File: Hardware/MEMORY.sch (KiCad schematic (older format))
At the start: 9 parts, among them J37 Micro_SD_Card, U45 M24C64-WDW6TP

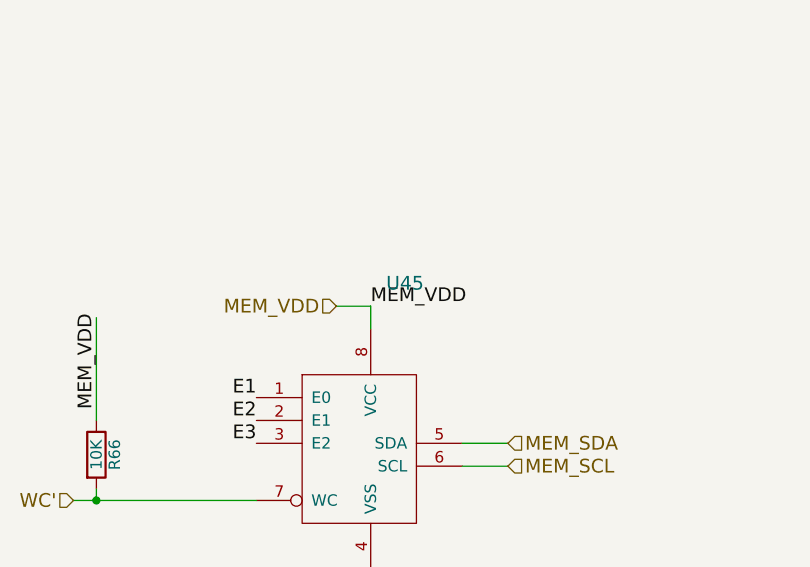
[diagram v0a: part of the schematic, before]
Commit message: Finished RLC bom stuff
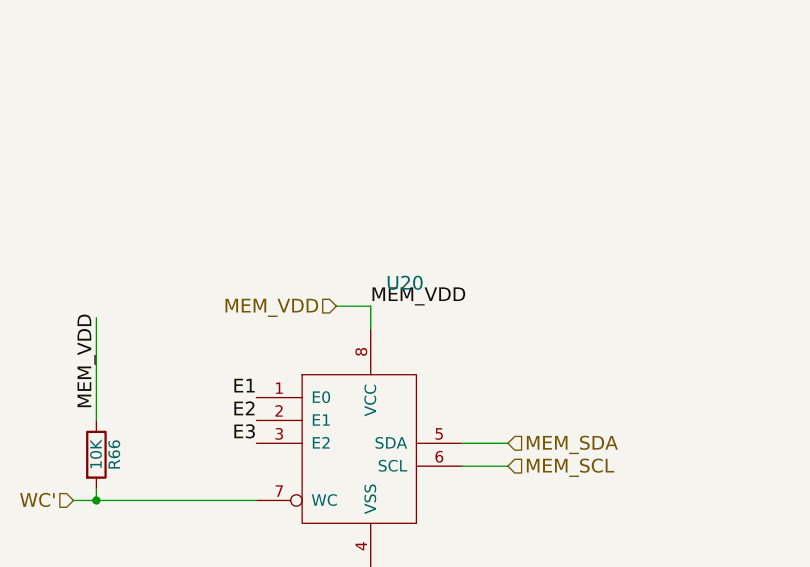
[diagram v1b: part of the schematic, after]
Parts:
- R60, R62, R64: part_num (none) -> RESS-001
- R61, R63, R65, R66: part_num (none) -> RESS-005
- renumbered U45 to U20
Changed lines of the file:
@@
 	7300 2100 7300 2400
 $Comp
-L M24C64-WDW6TP U45
+L M24C64-WDW6TP U20
 U 1 1 592069C1
 P 5300 5000
-F 0 "U45" H 5300 5450 60  0000 C CNN
+F 0 "U20" H 5300 5450 60  0000 C CNN
 F 1 "M24C64-WDW6TP" H 5250 4100 60  0000 C CNN
 F 2 "" H 5300 5000 60  0001 C CNN
@@
 Text HLabel 3850 5500 0    60   Input ~ 0
 WC'
-$Comp
-L R R66
-U 1 1 59206A6D
-P 3950 5300
-F 0 "R66" V 4030 5300 50  0000 C CNN
-F 1 "10K" V 3950 5300 50  0000 C CNN
-F 2 "" V 3880 5300 50  0001 C CNN
-F 3 "" H 3950 5300 50  0001 C CNN
-	1    3950 5300
-	1    0    0    -1
-$EndComp
 Wire Wire Line
 	3950 5450 3950 5500
@@
 F 2 "" V 1580 5650 50  0001 C CNN
 F 3 "" H 1650 5650 50  0001 C CNN
+F 4 "RESS-005" V 1650 5650 60  0001 C CNN "part_num"
 	1    1650 5650
-	1    0    0    -1
-$EndComp
-$Comp
-L R R63
-U 1 1 59206CAA
-P 1900 5650
-F 0 "R63" V 1980 5650 50  0000 C CNN
-F 1 "10K" V 1900 5650 50  0000 C CNN
-F 2 "" V 1830 5650 50  0001 C CNN
-F 3 "" H 1900 5650 50  0001 C CNN
-	1    1900 5650
-	1    0    0    -1
-$EndComp
-$Comp
-L R R65
-U 1 1 59206CD2
-P 2150 5650
-F 0 "R65" V 2230 5650 50  0000 C CNN
-F 1 "10K" V 2150 5650 50  0000 C CNN
-F 2 "" V 2080 5650 50  0001 C CNN
-F 3 "" H 2150 5650 50  0001 C CNN
-	1    2150 5650
 	1    0    0    -1
 $EndComp
@@
 F 2 "" V 1580 5100 50  0001 C CNN
 F 3 "" H 1650 5100 50  0001 C CNN
+F 4 "RESS-001" V 1650 5100 60  0001 C CNN "part_num"
 	1    1650 5100
-	1    0    0    -1
-$EndComp
-$Comp
-L R R62
-U 1 1 59206D6A
-P 1900 5100
-F 0 "R62" V 1980 5100 50  0000 C CNN
-F 1 "0" V 1900 5100 50  0000 C CNN
-F 2 "" V 1830 5100 50  0001 C CNN
-F 3 "" H 1900 5100 50  0001 C CNN
-	1    1900 5100
-	1    0    0    -1
-$EndComp
-$Comp
-L R R64
-U 1 1 59206D71
-P 2150 5100
-F 0 "R64" V 2230 5100 50  0000 C CNN
-F 1 "0" V 2150 5100 50  0000 C CNN
-F 2 "" V 2080 5100 50  0001 C CNN
-F 3 "" H 2150 5100 50  0001 C CNN
-	1    2150 5100
 	1    0    0    -1
 $EndComp
@@
 	1    0    0    -1
 $EndComp
+$Comp
+L R R63
+U 1 1 59596B34
+P 1900 5650
+F 0 "R63" V 1980 5650 50  0000 C CNN
+F 1 "10K" V 1900 5650 50  0000 C CNN
+F 2 "" V 1830 5650 50  0001 C CNN
+F 3 "" H 1900 5650 50  0001 C CNN
+F 4 "RESS-005" V 1900 5650 60  0001 C CNN "part_num"
+	1    1900 5650
+	1    0    0    -1
+$EndComp
+$Comp
+L R R65
+U 1 1 59596B68
+P 2150 5650
+F 0 "R65" V 2230 5650 50  0000 C CNN
+F 1 "10K" V 2150 5650 50  0000 C CNN
+F 2 "" V 2080 5650 50  0001 C CNN
+F 3 "" H 2150 5650 50  0001 C CNN
+F 4 "RESS-005" V 2150 5650 60  0001 C CNN "part_num"
+	1    2150 5650
+	1    0    0    -1
+$EndComp
+$Comp
+L R R62
+U 1 1 59596BE6
+P 1900 5100
+F 0 "R62" V 1980 5100 50  0000 C CNN
+F 1 "0" V 1900 5100 50  0000 C CNN
+F 2 "" V 1830 5100 50  0001 C CNN
+F 3 "" H 1900 5100 50  0001 C CNN
+F 4 "RESS-001" V 1900 5100 60  0001 C CNN "part_num"
+	1    1900 5100
+	1    0    0    -1
+$EndComp
+$Comp
+L R R64
+U 1 1 59596C1A
+P 2150 5100
+F 0 "R64" V 2230 5100 50  0000 C CNN
+F 1 "0" V 2150 5100 50  0000 C CNN
+F 2 "" V 2080 5100 50  0001 C CNN
+F 3 "" H 2150 5100 50  0001 C CNN
+F 4 "RESS-001" V 2150 5100 60  0001 C CNN "part_num"
+	1    2150 5100
+	1    0    0    -1
+$EndComp
+$Comp
+L R R66
+U 1 1 59596D32
+P 3950 5300
+F 0 "R66" V 4030 5300 50  0000 C CNN
+F 1 "10K" V 3950 5300 50  0000 C CNN
+F 2 "" V 3880 5300 50  0001 C CNN
+F 3 "" H 3950 5300 50  0001 C CNN
+F 4 "RESS-005" V 3950 5300 60  0001 C CNN "part_num"
+	1    3950 5300
+	1    0    0    -1
+$EndComp

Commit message: Added ressistor footprint
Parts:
- R60, R61, R62, R63, R64, R65, R66: footprint (none) -> Resistors_SMD:R_0603_HandSoldering
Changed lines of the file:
@@
 F 0 "R61" V 1730 5650 50  0000 C CNN
 F 1 "10K" V 1650 5650 50  0000 C CNN
-F 2 "" V 1580 5650 50  0001 C CNN
+F 2 "Resistors_SMD:R_0603_HandSoldering" V 1580 5650 50  0001 C CNN
 F 3 "" H 1650 5650 50  0001 C CNN
 F 4 "RESS-005" V 1650 5650 60  0001 C CNN "part_num"
@@
 F 0 "R60" V 1730 5100 50  0000 C CNN
 F 1 "0" V 1650 5100 50  0000 C CNN
-F 2 "" V 1580 5100 50  0001 C CNN
+F 2 "Resistors_SMD:R_0603_HandSoldering" V 1580 5100 50  0001 C CNN
 F 3 "" H 1650 5100 50  0001 C CNN
 F 4 "RESS-001" V 1650 5100 60  0001 C CNN "part_num"
@@
 F 0 "R63" V 1980 5650 50  0000 C CNN
 F 1 "10K" V 1900 5650 50  0000 C CNN
-F 2 "" V 1830 5650 50  0001 C CNN
+F 2 "Resistors_SMD:R_0603_HandSoldering" V 1830 5650 50  0001 C CNN
 F 3 "" H 1900 5650 50  0001 C CNN
 F 4 "RESS-005" V 1900 5650 60  0001 C CNN "part_num"
@@
 F 0 "R65" V 2230 5650 50  0000 C CNN
 F 1 "10K" V 2150 5650 50  0000 C CNN
-F 2 "" V 2080 5650 50  0001 C CNN
+F 2 "Resistors_SMD:R_0603_HandSoldering" V 2080 5650 50  0001 C CNN
 F 3 "" H 2150 5650 50  0001 C CNN
 F 4 "RESS-005" V 2150 5650 60  0001 C CNN "part_num"
@@
 F 0 "R62" V 1980 5100 50  0000 C CNN
 F 1 "0" V 1900 5100 50  0000 C CNN
-F 2 "" V 1830 5100 50  0001 C CNN
+F 2 "Resistors_SMD:R_0603_HandSoldering" V 1830 5100 50  0001 C CNN
 F 3 "" H 1900 5100 50  0001 C CNN
 F 4 "RESS-001" V 1900 5100 60  0001 C CNN "part_num"
@@
 F 0 "R64" V 2230 5100 50  0000 C CNN
 F 1 "0" V 2150 5100 50  0000 C CNN
-F 2 "" V 2080 5100 50  0001 C CNN
+F 2 "Resistors_SMD:R_0603_HandSoldering" V 2080 5100 50  0001 C CNN
 F 3 "" H 2150 5100 50  0001 C CNN
 F 4 "RESS-001" V 2150 5100 60  0001 C CNN "part_num"
@@
 F 0 "R66" V 4030 5300 50  0000 C CNN
 F 1 "10K" V 3950 5300 50  0000 C CNN
-F 2 "" V 3880 5300 50  0001 C CNN
+F 2 "Resistors_SMD:R_0603_HandSoldering" V 3880 5300 50  0001 C CNN
 F 3 "" H 3950 5300 50  0001 C CNN
 F 4 "RESS-005" V 3950 5300 60  0001 C CNN "part_num"

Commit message: PCB?!
Added initial PCB file with ratsnest. footprint library still needs to
be setup.
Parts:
- U20: footprint (none) -> Housings_SSOP:TSSOP-8_4.4x3mm_Pitch0.65mm
- renumbered R60 to R85, R61 to R86, R62 to R87, R63 to R88, R64 to R89, R65 to R90, R66 to R91
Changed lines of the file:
@@
 $EndDescr
 $Comp
-L GND #PWR054
+L GND #PWR55
 U 1 1 5920672F
 P 9100 2500
-F 0 "#PWR054" H 9100 2250 50  0001 C CNN
+F 0 "#PWR55" H 9100 2250 50  0001 C CNN
 F 1 "GND" H 9100 2350 50  0000 C CNN
 F 2 "" H 9100 2500 50  0001 C CNN
@@
 	6950 2200 7400 2200
 $Comp
-L GND #PWR055
+L GND #PWR54
 U 1 1 592067B5
 P 7300 2400
-F 0 "#PWR055" H 7300 2150 50  0001 C CNN
+F 0 "#PWR54" H 7300 2150 50  0001 C CNN
 F 1 "GND" H 7300 2250 50  0000 C CNN
 F 2 "" H 7300 2400 50  0001 C CNN
@@
 	7300 2100 7300 2400
 $Comp
-L M24C64-WDW6TP U20
-U 1 1 592069C1
-P 5300 5000
-F 0 "U20" H 5300 5450 60  0000 C CNN
-F 1 "M24C64-WDW6TP" H 5250 4100 60  0000 C CNN
-F 2 "" H 5300 5000 60  0001 C CNN
-F 3 "" H 5300 5450 60  0001 C CNN
-F 4 "MEMM-001" H 5300 5000 60  0001 C CNN "part_num"
-	1    5300 5000
-	1    0    0    -1
-$EndComp
-$Comp
-L GND #PWR056
+L GND #PWR53
 U 1 1 592069E4
 P 5150 5850
-F 0 "#PWR056" H 5150 5600 50  0001 C CNN
+F 0 "#PWR53" H 5150 5600 50  0001 C CNN
 F 1 "GND" H 5150 5700 50  0000 C CNN
 F 2 "" H 5150 5850 50  0001 C CNN
@@
 E3
 $Comp
-L R R61
+L R R86
 U 1 1 59206C6F
 P 1650 5650
-F 0 "R61" V 1730 5650 50  0000 C CNN
+F 0 "R86" V 1730 5650 50  0000 C CNN
 F 1 "10K" V 1650 5650 50  0000 C CNN
 F 2 "Resistors_SMD:R_0603_HandSoldering" V 1580 5650 50  0001 C CNN
@@
 $EndComp
 $Comp
-L R R60
+L R R85
 U 1 1 59206D63
 P 1650 5100
-F 0 "R60" V 1730 5100 50  0000 C CNN
+F 0 "R85" V 1730 5100 50  0000 C CNN
 F 1 "0" V 1650 5100 50  0000 C CNN
 F 2 "Resistors_SMD:R_0603_HandSoldering" V 1580 5100 50  0001 C CNN
@@
 	2150 5250 2150 5500
 $Comp
-L GND #PWR057
+L GND #PWR52
 U 1 1 59206DDE
 P 1900 5950
-F 0 "#PWR057" H 1900 5700 50  0001 C CNN
+F 0 "#PWR52" H 1900 5700 50  0001 C CNN
 F 1 "GND" H 1900 5800 50  0000 C CNN
 F 2 "" H 1900 5950 50  0001 C CNN
@@
 $EndComp
 $Comp
-L R R63
+L R R88
 U 1 1 59596B34
 P 1900 5650
-F 0 "R63" V 1980 5650 50  0000 C CNN
+F 0 "R88" V 1980 5650 50  0000 C CNN
 F 1 "10K" V 1900 5650 50  0000 C CNN
 F 2 "Resistors_SMD:R_0603_HandSoldering" V 1830 5650 50  0001 C CNN
@@
 $EndComp
 $Comp
-L R R65
+L R R90
 U 1 1 59596B68
 P 2150 5650
-F 0 "R65" V 2230 5650 50  0000 C CNN
+F 0 "R90" V 2230 5650 50  0000 C CNN
 F 1 "10K" V 2150 5650 50  0000 C CNN
 F 2 "Resistors_SMD:R_0603_HandSoldering" V 2080 5650 50  0001 C CNN
@@
 $EndComp
 $Comp
-L R R62
+L R R87
 U 1 1 59596BE6
 P 1900 5100
-F 0 "R62" V 1980 5100 50  0000 C CNN
+F 0 "R87" V 1980 5100 50  0000 C CNN
 F 1 "0" V 1900 5100 50  0000 C CNN
 F 2 "Resistors_SMD:R_0603_HandSoldering" V 1830 5100 50  0001 C CNN
@@
 $EndComp
 $Comp
-L R R64
+L R R89
 U 1 1 59596C1A
 P 2150 5100
-F 0 "R64" V 2230 5100 50  0000 C CNN
+F 0 "R89" V 2230 5100 50  0000 C CNN
 F 1 "0" V 2150 5100 50  0000 C CNN
 F 2 "Resistors_SMD:R_0603_HandSoldering" V 2080 5100 50  0001 C CNN
@@
 $EndComp
 $Comp
-L R R66
+L R R91
 U 1 1 59596D32
 P 3950 5300
-F 0 "R66" V 4030 5300 50  0000 C CNN
+F 0 "R91" V 4030 5300 50  0000 C CNN
 F 1 "10K" V 3950 5300 50  0000 C CNN
 F 2 "Resistors_SMD:R_0603_HandSoldering" V 3880 5300 50  0001 C CNN
@@
 	1    0    0    -1
 $EndComp
+$Comp
+L M24C64-WDW6TP U20
+U 1 1 595FB585
+P 5300 5000
+F 0 "U20" H 5300 5450 60  0000 C CNN
+F 1 "M24C64-WDW6TP" H 5250 4100 60  0000 C CNN
+F 2 "Housings_SSOP:TSSOP-8_4.4x3mm_Pitch0.65mm" H 5200 5350 60  0001 C CNN
+F 3 "" H 5300 5450 60  0001 C CNN
+F 4 "MEMM-001" H 5400 5550 60  0001 C CNN "part_num"
+	1    5300 5000
+	1    0    0    -1
+$EndComp

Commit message: commit before my computer restarts
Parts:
- J37: footprint (none) -> Pin_Headers:Pin_Header_Angled_1x09_Pitch2.54mm
- renumbered R85 to R41, R86 to R42, R87 to R43, R88 to R44, R89 to R45, R90 to R46, R91 to R47
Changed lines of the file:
@@
 E3
 $Comp
-L R R86
+L R R42
 U 1 1 59206C6F
 P 1650 5650
-F 0 "R86" V 1730 5650 50  0000 C CNN
+F 0 "R42" V 1730 5650 50  0000 C CNN
 F 1 "10K" V 1650 5650 50  0000 C CNN
 F 2 "Resistors_SMD:R_0603_HandSoldering" V 1580 5650 50  0001 C CNN
@@
 $EndComp
 $Comp
-L R R85
+L R R41
 U 1 1 59206D63
 P 1650 5100
-F 0 "R85" V 1730 5100 50  0000 C CNN
+F 0 "R41" V 1730 5100 50  0000 C CNN
 F 1 "0" V 1650 5100 50  0000 C CNN
 F 2 "Resistors_SMD:R_0603_HandSoldering" V 1580 5100 50  0001 C CNN
@@
 F 0 "J37" H 7650 2500 50  0000 C CNN
 F 1 "Micro_SD_Card" H 8950 2500 50  0000 R CNN
-F 2 "" H 9450 2200 50  0001 C CNN
+F 2 "Pin_Headers:Pin_Header_Angled_1x09_Pitch2.54mm" H 9450 2200 50  0001 C CNN
 F 3 "" H 8300 1900 50  0001 C CNN
 F 4 "MEMM-002" H 8300 1900 60  0001 C CNN "part_num"
@@
 $EndComp
 $Comp
-L R R88
+L R R44
 U 1 1 59596B34
 P 1900 5650
-F 0 "R88" V 1980 5650 50  0000 C CNN
+F 0 "R44" V 1980 5650 50  0000 C CNN
 F 1 "10K" V 1900 5650 50  0000 C CNN
 F 2 "Resistors_SMD:R_0603_HandSoldering" V 1830 5650 50  0001 C CNN
@@
 $EndComp
 $Comp
-L R R90
+L R R46
 U 1 1 59596B68
 P 2150 5650
-F 0 "R90" V 2230 5650 50  0000 C CNN
+F 0 "R46" V 2230 5650 50  0000 C CNN
 F 1 "10K" V 2150 5650 50  0000 C CNN
 F 2 "Resistors_SMD:R_0603_HandSoldering" V 2080 5650 50  0001 C CNN
@@
 $EndComp
 $Comp
-L R R87
+L R R43
 U 1 1 59596BE6
 P 1900 5100
-F 0 "R87" V 1980 5100 50  0000 C CNN
+F 0 "R43" V 1980 5100 50  0000 C CNN
 F 1 "0" V 1900 5100 50  0000 C CNN
 F 2 "Resistors_SMD:R_0603_HandSoldering" V 1830 5100 50  0001 C CNN
@@
 $EndComp
 $Comp
-L R R89
+L R R45
 U 1 1 59596C1A
 P 2150 5100
-F 0 "R89" V 2230 5100 50  0000 C CNN
+F 0 "R45" V 2230 5100 50  0000 C CNN
 F 1 "0" V 2150 5100 50  0000 C CNN
 F 2 "Resistors_SMD:R_0603_HandSoldering" V 2080 5100 50  0001 C CNN
@@
 $EndComp
 $Comp
-L R R91
+L R R47
 U 1 1 59596D32
 P 3950 5300
-F 0 "R91" V 4030 5300 50  0000 C CNN
+F 0 "R47" V 4030 5300 50  0000 C CNN
 F 1 "10K" V 3950 5300 50  0000 C CNN
 F 2 "Resistors_SMD:R_0603_HandSoldering" V 3880 5300 50  0001 C CNN

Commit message: imported micro sd footprint
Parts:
- J37: footprint Pin_Headers:Pin_Header_Angled_1x09_Pitch2.54mm -> WARG:micro_sd
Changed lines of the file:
@@
 $EndDescr
 $Comp
-L GND #PWR054
+L GND #PWR056
 U 1 1 5920672F
 P 9100 2500
-F 0 "#PWR054" H 9100 2250 50  0001 C CNN
+F 0 "#PWR056" H 9100 2250 50  0001 C CNN
 F 1 "GND" H 9100 2350 50  0000 C CNN
 F 2 "" H 9100 2500 50  0001 C CNN
@@
 	6950 2200 7400 2200
 $Comp
-L GND #PWR055
+L GND #PWR057
 U 1 1 592067B5
 P 7300 2400
-F 0 "#PWR055" H 7300 2150 50  0001 C CNN
+F 0 "#PWR057" H 7300 2150 50  0001 C CNN
 F 1 "GND" H 7300 2250 50  0000 C CNN
 F 2 "" H 7300 2400 50  0001 C CNN
@@
 	7300 2100 7300 2400
 $Comp
-L GND #PWR056
+L GND #PWR058
 U 1 1 592069E4
 P 5150 5850
-F 0 "#PWR056" H 5150 5600 50  0001 C CNN
+F 0 "#PWR058" H 5150 5600 50  0001 C CNN
 F 1 "GND" H 5150 5700 50  0000 C CNN
 F 2 "" H 5150 5850 50  0001 C CNN
@@
 	2150 5250 2150 5500
 $Comp
-L GND #PWR057
+L GND #PWR059
 U 1 1 59206DDE
 P 1900 5950
-F 0 "#PWR057" H 1900 5700 50  0001 C CNN
+F 0 "#PWR059" H 1900 5700 50  0001 C CNN
 F 1 "GND" H 1900 5800 50  0000 C CNN
 F 2 "" H 1900 5950 50  0001 C CNN
@@
 F 0 "J37" H 7650 2500 50  0000 C CNN
 F 1 "Micro_SD_Card" H 8950 2500 50  0000 R CNN
-F 2 "Pin_Headers:Pin_Header_Angled_1x09_Pitch2.54mm" H 9450 2200 50  0001 C CNN
+F 2 "WARG:micro_sd" H 9450 2200 50  0001 C CNN
 F 3 "" H 8300 1900 50  0001 C CNN
 F 4 "MEMM-002" H 8300 1900 60  0001 C CNN "part_num"

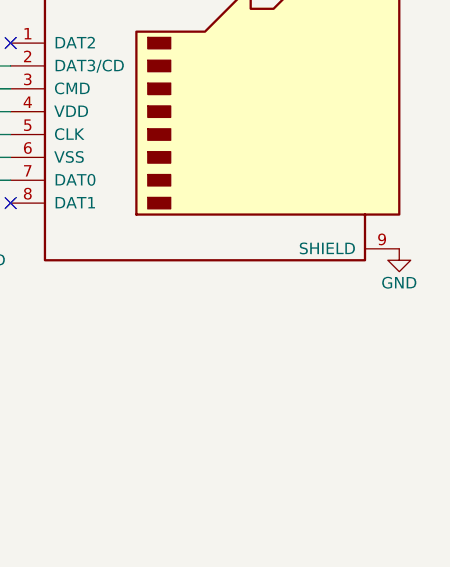
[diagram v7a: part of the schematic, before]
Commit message: Updated sd card footprint with shield pin
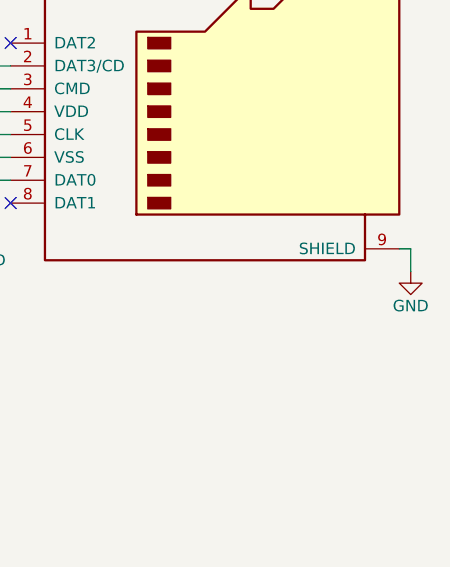
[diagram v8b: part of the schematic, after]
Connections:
- wire segments 26 -> 28
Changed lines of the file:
@@
 L GND #PWR056
 U 1 1 5920672F
-P 9100 2500
-F 0 "#PWR056" H 9100 2250 50  0001 C CNN
-F 1 "GND" H 9100 2350 50  0000 C CNN
-F 2 "" H 9100 2500 50  0001 C CNN
-F 3 "" H 9100 2500 50  0001 C CNN
-	1    9100 2500
+P 9150 2600
+F 0 "#PWR056" H 9150 2350 50  0001 C CNN
+F 1 "GND" H 9150 2450 50  0000 C CNN
+F 2 "" H 9150 2600 50  0001 C CNN
+F 3 "" H 9150 2600 50  0001 C CNN
+	1    9150 2600
 	1    0    0    -1
 $EndComp
@@
 Text HLabel 6950 1700 0    60   Input ~ 0
 SD_CS
-Wire Wire Line
-	6950 1700 7400 1700
-Wire Wire Line
-	7400 1800 6950 1800
-Wire Wire Line
-	7400 2000 6950 2000
-Wire Wire Line
-	6950 2200 7400 2200
 $Comp
 L GND #PWR057
@@
 	1    0    0    -1
 $EndComp
-Wire Wire Line
-	7300 2100 7400 2100
-Wire Wire Line
-	7300 2100 7300 2400
 $Comp
 L GND #PWR058
@@
 	1    0    0    -1
 $EndComp
-Wire Wire Line
-	5150 5850 5150 5800
 Text HLabel 5000 4650 0    60   Input ~ 0
 MEM_VDD
-Wire Wire Line
-	5000 4650 5150 4650
-Wire Wire Line
-	5150 4650 5150 4750
 Text HLabel 5750 5250 2    60   Input ~ 0
 MEM_SDA
 Text HLabel 5750 5350 2    60   Input ~ 0
 MEM_SCL
-Wire Wire Line
-	5750 5250 5550 5250
-Wire Wire Line
-	5550 5350 5750 5350
-Wire Wire Line
-	3850 5500 4650 5500
 Text HLabel 3850 5500 0    60   Input ~ 0
 WC'
-Wire Wire Line
-	3950 5450 3950 5500
-Connection ~ 3950 5500
-Wire Wire Line
-	3950 4700 3950 5150
 Text Label 5150 4650 0    60   ~ 0
 MEM_VDD
@@
 	1    0    0    -1
 $EndComp
-Wire Wire Line
-	1650 5250 1650 5500
-Wire Wire Line
-	1900 5250 1900 5500
-Wire Wire Line
-	2150 5250 2150 5500
 $Comp
 L GND #PWR059
@@
 	1    0    0    -1
 $EndComp
-Wire Wire Line
-	1650 5800 1650 5900
-Wire Wire Line
-	1650 5900 2150 5900
-Wire Wire Line
-	2150 5900 2150 5800
-Wire Wire Line
-	1900 5800 1900 5950
-Connection ~ 1900 5900
 Text Label 1900 4800 0    60   ~ 0
 MEM_VDD
-Wire Wire Line
-	1650 4800 2150 4800
-Wire Wire Line
-	1650 4800 1650 4950
-Wire Wire Line
-	2150 4800 2150 4950
-Wire Wire Line
-	1900 4950 1900 4800
-Connection ~ 1900 4800
 Text Label 1650 5400 0    60   ~ 0
 E1
@@
 NoConn ~ 7400 1600
 NoConn ~ 7400 2300
-Wire Wire Line
-	7400 1900 6950 1900
 $Comp
 L Micro_SD_Card J37
@@
 	1    0    0    -1
 $EndComp
+Wire Wire Line
+	6950 1700 7400 1700
+Wire Wire Line
+	7400 1800 6950 1800
+Wire Wire Line
+	7400 2000 6950 2000
+Wire Wire Line
+	6950 2200 7400 2200
+Wire Wire Line
+	7300 2100 7400 2100
+Wire Wire Line
+	7300 2100 7300 2400
+Wire Wire Line
+	5150 5850 5150 5800
+Wire Wire Line
+	5000 4650 5150 4650
+Wire Wire Line
+	5150 4650 5150 4750
+Wire Wire Line
+	5750 5250 5550 5250
+Wire Wire Line
+	5550 5350 5750 5350
+Wire Wire Line
+	3850 5500 4650 5500
+Wire Wire Line
+	3950 5450 3950 5500
+Connection ~ 3950 5500
+Wire Wire Line
+	3950 4700 3950 5150
+Wire Wire Line
+	1650 5250 1650 5500
+Wire Wire Line
+	1900 5250 1900 5500
+Wire Wire Line
+	2150 5250 2150 5500
+Wire Wire Line
+	1650 5800 1650 5900
+Wire Wire Line
+	1650 5900 2150 5900
+Wire Wire Line
+	2150 5900 2150 5800
+Wire Wire Line
+	1900 5800 1900 5950
+Connection ~ 1900 5900
+Wire Wire Line
+	1650 4800 2150 4800
+Wire Wire Line
+	1650 4800 1650 4950
+Wire Wire Line
+	2150 4800 2150 4950
+Wire Wire Line
+	1900 4950 1900 4800
+Connection ~ 1900 4800
+Wire Wire Line
+	7400 1900 6950 1900
+Wire Wire Line
+	9150 2600 9150 2500
+Wire Wire Line
+	9150 2500 9100 2500
 $EndSCHEMATC
